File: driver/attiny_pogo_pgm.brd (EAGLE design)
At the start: 26.9 x 17.3 mm, 9 parts, among them IC1 ATTiny85, J1 AVR_SPI_PRG_6NS, P5V TPTP10R

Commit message: prepare for routing
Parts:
- removed IC1: ATTiny85, atmel:8S2
- moved JP1 9.60 mm to (11.3, 2.41), turned to 90 degrees
- moved J1 3.79 mm to (5.21, 3.68)
- moved PMOSI 3.69 mm to (2.29, 12.4)
- moved PSCK 3.69 mm to (2.29, 9.91)
- moved P5V 3.69 mm to (1.65, 8.64)
- moved PGND 3.69 mm to (9.02, 12.4)
- moved PMISO 3.69 mm to (1.65, 11.2)
- moved PRESET 3.69 mm to (9.02, 8.64)
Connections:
- net +5V: no longer IC1.8
- net GND: no longer IC1.4
- net IN1/MISO: no longer IC1.6
- net RESET-: no longer IC1.1
- net SCL/SCK: no longer IC1.7
- net SDA/MOSI: no longer IC1.5
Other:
- board size 26.9 x 17.3 mm -> 14.3 x 14.8 mm
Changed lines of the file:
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@@
 <board>
 <plain>
-<wire x1="0" y1="0" x2="26.904" y2="0" width="0" layer="20"/>
-<wire x1="26.904" y1="0" x2="26.904" y2="17.323" width="0" layer="20"/>
-<wire x1="26.904" y1="17.323" x2="0" y2="17.323" width="0" layer="20"/>
-<wire x1="0" y1="17.323" x2="0" y2="0" width="0" layer="20"/>
+<wire x1="0" y1="0" x2="14.331" y2="0" width="0" layer="20"/>
+<wire x1="14.331" y1="0" x2="14.331" y2="14.783" width="0" layer="20"/>
+<wire x1="14.331" y1="14.783" x2="0" y2="14.783" width="0" layer="20"/>
+<wire x1="0" y1="14.783" x2="0" y2="0" width="0" layer="20"/>
 </plain>
 <attributes>
@@
 </autorouter>
 <elements>
-<element name="IC1" library="atmel" package="8S2" value="ATTiny85" x="9.144" y="10.668" rot="R90">
-<attribute name="OC_NEWARK" value="96K6522" x="14.224" y="37.338" size="1.778" layer="27" rot="R90" display="off"/>
-<attribute name="MPN" value="ATTINY13-20SU" x="14.224" y="37.338" size="1.778" layer="27" rot="R90" display="off"/>
-<attribute name="MF" value="" x="14.224" y="37.338" size="1.778" layer="27" rot="R90" display="off"/>
-<attribute name="OC_FARNELL" value="9171568" x="14.224" y="37.338" size="1.778" layer="27" rot="R90" display="off"/>
-</element>
-<element name="J1" library="SparkFun-Connectors" package="2X3-NS" value="AVR_SPI_PRG_6NS" x="8.89" y="4.572"/>
-<element name="JP1" library="SparkFun-Connectors" package="1X02" value="" x="2.286" y="5.715" rot="R270"/>
-<element name="PMOSI" library="testpad" package="TP10R" value="TPTP10R" x="5.969" y="12.573">
-<attribute name="TP_SIGNAL_NAME" value="" x="5.969" y="12.573" size="1.778" layer="27" display="off"/>
-</element>
-<element name="PRESET" library="testpad" package="TP10R" value="TPTP10R" x="12.7" y="8.763">
-<attribute name="TP_SIGNAL_NAME" value="" x="12.7" y="8.763" size="1.778" layer="27" display="off"/>
-</element>
-<element name="PSCK" library="testpad" package="TP10R" value="TPTP10R" x="5.969" y="10.033">
-<attribute name="TP_SIGNAL_NAME" value="" x="5.969" y="10.033" size="1.778" layer="27" display="off"/>
-</element>
-<element name="PMISO" library="testpad" package="TP10R" value="TPTP10R" x="5.334" y="11.303">
-<attribute name="TP_SIGNAL_NAME" value="" x="5.334" y="11.303" size="1.778" layer="27" display="off"/>
-</element>
-<element name="PGND" library="testpad" package="TP10R" value="TPTP10R" x="12.7" y="12.573">
-<attribute name="TP_SIGNAL_NAME" value="" x="12.7" y="12.573" size="1.778" layer="27" display="off"/>
-</element>
-<element name="P5V" library="testpad" package="TP10R" value="TPTP10R" x="5.334" y="8.763">
-<attribute name="TP_SIGNAL_NAME" value="" x="5.334" y="8.763" size="1.778" layer="27" display="off"/>
+<element name="J1" library="SparkFun-Connectors" package="2X3-NS" value="AVR_SPI_PRG_6NS" x="5.207" y="3.683"/>
+<element name="JP1" library="SparkFun-Connectors" package="1X02" value="" x="11.303" y="2.413" rot="R90"/>
+<element name="PMOSI" library="testpad" package="TP10R" value="TPTP10R" x="2.286" y="12.446">
+<attribute name="TP_SIGNAL_NAME" value="" x="2.286" y="12.446" size="1.778" layer="27" display="off"/>
+</element>
+<element name="PRESET" library="testpad" package="TP10R" value="TPTP10R" x="9.017" y="8.636">
+<attribute name="TP_SIGNAL_NAME" value="" x="9.017" y="8.636" size="1.778" layer="27" display="off"/>
+</element>
+<element name="PSCK" library="testpad" package="TP10R" value="TPTP10R" x="2.286" y="9.906">
+<attribute name="TP_SIGNAL_NAME" value="" x="2.286" y="9.906" size="1.778" layer="27" display="off"/>
+</element>
+<element name="PMISO" library="testpad" package="TP10R" value="TPTP10R" x="1.651" y="11.176">
+<attribute name="TP_SIGNAL_NAME" value="" x="1.651" y="11.176" size="1.778" layer="27" display="off"/>
+</element>
+<element name="PGND" library="testpad" package="TP10R" value="TPTP10R" x="9.017" y="12.446">
+<attribute name="TP_SIGNAL_NAME" value="" x="9.017" y="12.446" size="1.778" layer="27" display="off"/>
+</element>
+<element name="P5V" library="testpad" package="TP10R" value="TPTP10R" x="1.651" y="8.636">
+<attribute name="TP_SIGNAL_NAME" value="" x="1.651" y="8.636" size="1.778" layer="27" display="off"/>
 </element>
 </elements>
 <signals>
 <signal name="IN1/MISO">
-<contactref element="IC1" pad="6"/>
 <contactref element="J1" pad="1"/>
 <contactref element="PMISO" pad="TP"/>
-<wire x1="5.334" y1="11.303" x2="5.74" y2="11.303" width="0" layer="19" extent="1-1"/>
-<wire x1="6.35" y1="3.302" x2="5.74" y2="11.303" width="0" layer="19" extent="1-1"/>
+<wire x1="2.667" y1="2.413" x2="1.651" y2="11.176" width="0" layer="19" extent="1-1"/>
 </signal>
 <signal name="GND">
-<contactref element="IC1" pad="4"/>
 <contactref element="J1" pad="6"/>
 <polygon width="0.2032" layer="1" isolate="0.4064">
@@
 </signal>
 <signal name="+5V">
-<contactref element="IC1" pad="8"/>
 <contactref element="J1" pad="2"/>
 <contactref element="JP1" pad="1"/>
 <contactref element="P5V" pad="TP"/>
-<wire x1="5.334" y1="8.763" x2="5.74" y2="8.763" width="0" layer="19" extent="1-1"/>
-<wire x1="6.35" y1="5.842" x2="5.74" y2="8.763" width="0" layer="19" extent="1-1"/>
-<wire x1="2.286" y1="5.715" x2="6.35" y2="5.842" width="0" layer="19" extent="1-1"/>
+<wire x1="2.667" y1="4.953" x2="11.303" y2="2.413" width="0" layer="19" extent="1-1"/>
+<wire x1="1.651" y1="8.636" x2="2.667" y2="4.953" width="0" layer="19" extent="1-1"/>
 </signal>
 <signal name="SDA/MOSI">
-<contactref element="IC1" pad="5"/>
 <contactref element="J1" pad="4"/>
 <contactref element="PMOSI" pad="TP"/>
-<wire x1="5.969" y1="12.573" x2="5.74" y2="12.573" width="0" layer="19" extent="1-1"/>
-<wire x1="8.89" y1="5.842" x2="5.969" y2="12.573" width="0" layer="19" extent="1-1"/>
+<wire x1="5.207" y1="4.953" x2="2.286" y2="12.446" width="0" layer="19" extent="1-1"/>
 </signal>
 <signal name="RESET-">
-<contactref element="IC1" pad="1"/>
 <contactref element="J1" pad="5"/>
 <contactref element="PRESET" pad="TP"/>
-<wire x1="12.548" y1="8.763" x2="12.7" y2="8.763" width="0" layer="19" extent="1-1"/>
-<wire x1="11.43" y1="3.302" x2="12.548" y2="8.763" width="0" layer="19" extent="1-1"/>
+<wire x1="7.747" y1="2.413" x2="9.017" y2="8.636" width="0" layer="19" extent="1-1"/>
 </signal>
 <signal name="SCL/SCK">
-<contactref element="IC1" pad="7"/>
 <contactref element="J1" pad="3"/>
 <contactref element="PSCK" pad="TP"/>
-<wire x1="5.969" y1="10.033" x2="5.74" y2="10.033" width="0" layer="19" extent="1-1"/>
-<wire x1="8.89" y1="3.302" x2="5.969" y2="10.033" width="0" layer="19" extent="1-1"/>
+<wire x1="5.207" y1="2.413" x2="2.286" y2="9.906" width="0" layer="19" extent="1-1"/>
 </signal>
 </signals>

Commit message: routed
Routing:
- net IN1/MISO: track 0.00 -> 25.4 mm
- net +5V: track 0.00 -> 20.6 mm
- net GND: track 0.00 -> 15.9 mm
- net SCL/SCK: track 0.00 -> 8.70 mm
- net SDA/MOSI: track 0.00 -> 8.70 mm
- net RESET-: track 0.00 -> 6.75 mm
- removed copper zone on layer 1, net GND
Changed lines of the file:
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@@
 <param name="RoutingGrid" value="2.5mil"/>
 <param name="tpViaShape" value="round"/>
-<param name="PrefDir.1" value="-"/>
+<param name="PrefDir.1" value="|"/>
 <param name="PrefDir.2" value="0"/>
 <param name="PrefDir.3" value="0"/>
@@
 <contactref element="J1" pad="1"/>
 <contactref element="PMISO" pad="TP"/>
-<wire x1="2.667" y1="2.413" x2="1.651" y2="11.176" width="0" layer="19" extent="1-1"/>
+<wire x1="1.4605" y1="11.3665" x2="1.651" y2="11.176" width="0.2032" layer="1"/>
+<wire x1="0.8255" y1="12.2555" x2="1.4605" y2="11.3665" width="0.2032" layer="1"/>
+<wire x1="1.3335" y1="13.6525" x2="0.8255" y2="12.2555" width="0.2032" layer="1"/>
+<wire x1="6.477" y1="13.6525" x2="1.3335" y2="13.6525" width="0.2032" layer="1"/>
+<wire x1="6.477" y1="1.905" x2="6.477" y2="13.6525" width="0.2032" layer="1"/>
+<wire x1="5.715" y1="1.016" x2="6.477" y2="1.905" width="0.2032" layer="1"/>
+<wire x1="2.667" y1="1.016" x2="5.715" y2="1.016" width="0.2032" layer="1"/>
+<wire x1="2.667" y1="2.413" x2="2.667" y2="1.016" width="0.2032" layer="1"/>
 </signal>
 <signal name="GND">
 <contactref element="J1" pad="6"/>
-<polygon width="0.2032" layer="1" isolate="0.4064">
-<vertex x="0" y="16.256"/>
-<vertex x="0" y="0"/>
-<vertex x="26.924" y="0"/>
-<vertex x="26.924" y="16.256"/>
-</polygon>
 <contactref element="JP1" pad="2"/>
 <contactref element="PGND" pad="TP"/>
+<wire x1="7.747" y1="11.176" x2="9.017" y2="12.446" width="0.2032" layer="1"/>
+<wire x1="7.747" y1="4.953" x2="7.747" y2="10.9855" width="0.2032" layer="1"/>
+<wire x1="7.747" y1="10.9855" x2="7.747" y2="11.176" width="0.2032" layer="1"/>
+<wire x1="10.4775" y1="6.5405" x2="11.303" y2="4.953" width="0.2032" layer="1"/>
+<wire x1="10.4775" y1="9.5885" x2="10.4775" y2="6.5405" width="0.2032" layer="1"/>
+<wire x1="7.8105" y1="10.9855" x2="10.4775" y2="9.5885" width="0.2032" layer="1"/>
+<wire x1="7.8105" y1="10.9855" x2="7.747" y2="10.9855" width="0.2032" layer="1"/>
 </signal>
 <signal name="+5V">
@@
 <contactref element="JP1" pad="1"/>
 <contactref element="P5V" pad="TP"/>
-<wire x1="2.667" y1="4.953" x2="11.303" y2="2.413" width="0" layer="19" extent="1-1"/>
-<wire x1="1.651" y1="8.636" x2="2.667" y2="4.953" width="0" layer="19" extent="1-1"/>
+<wire x1="2.667" y1="7.62" x2="1.651" y2="8.636" width="0.2032" layer="1"/>
+<wire x1="2.667" y1="4.953" x2="2.667" y2="7.62" width="0.2032" layer="1"/>
+<wire x1="11.303" y1="2.413" x2="11.303" y2="1.651" width="0.2032" layer="1"/>
+<wire x1="11.303" y1="1.651" x2="10.16" y2="0.508" width="0.2032" layer="1"/>
+<wire x1="10.16" y1="0.508" x2="1.651" y2="0.508" width="0.2032" layer="1"/>
+<wire x1="1.651" y1="0.508" x2="0.762" y2="1.397" width="0.2032" layer="1"/>
+<wire x1="0.762" y1="1.397" x2="0.762" y2="3.048" width="0.2032" layer="1"/>
+<wire x1="0.762" y1="3.048" x2="2.667" y2="4.953" width="0.2032" layer="1"/>
 </signal>
 <signal name="SDA/MOSI">
 <contactref element="J1" pad="4"/>
 <contactref element="PMOSI" pad="TP"/>
-<wire x1="5.207" y1="4.953" x2="2.286" y2="12.446" width="0" layer="19" extent="1-1"/>
+<wire x1="5.207" y1="9.525" x2="2.286" y2="12.446" width="0.2032" layer="1"/>
+<wire x1="5.207" y1="4.953" x2="5.207" y2="9.525" width="0.2032" layer="1"/>
 </signal>
 <signal name="RESET-">
 <contactref element="J1" pad="5"/>
 <contactref element="PRESET" pad="TP"/>
-<wire x1="7.747" y1="2.413" x2="9.017" y2="8.636" width="0" layer="19" extent="1-1"/>
+<wire x1="9.017" y1="3.683" x2="9.017" y2="8.636" width="0.2032" layer="1"/>
+<wire x1="7.747" y1="2.413" x2="9.017" y2="3.683" width="0.2032" layer="1"/>
 </signal>
 <signal name="SCL/SCK">
 <contactref element="J1" pad="3"/>
 <contactref element="PSCK" pad="TP"/>
-<wire x1="5.207" y1="2.413" x2="2.286" y2="9.906" width="0" layer="19" extent="1-1"/>
+<wire x1="3.937" y1="8.255" x2="2.286" y2="9.906" width="0.2032" layer="1"/>
+<wire x1="3.937" y1="3.683" x2="3.937" y2="8.255" width="0.2032" layer="1"/>
+<wire x1="5.207" y1="2.413" x2="3.937" y2="3.683" width="0.2032" layer="1"/>
 </signal>
 </signals>

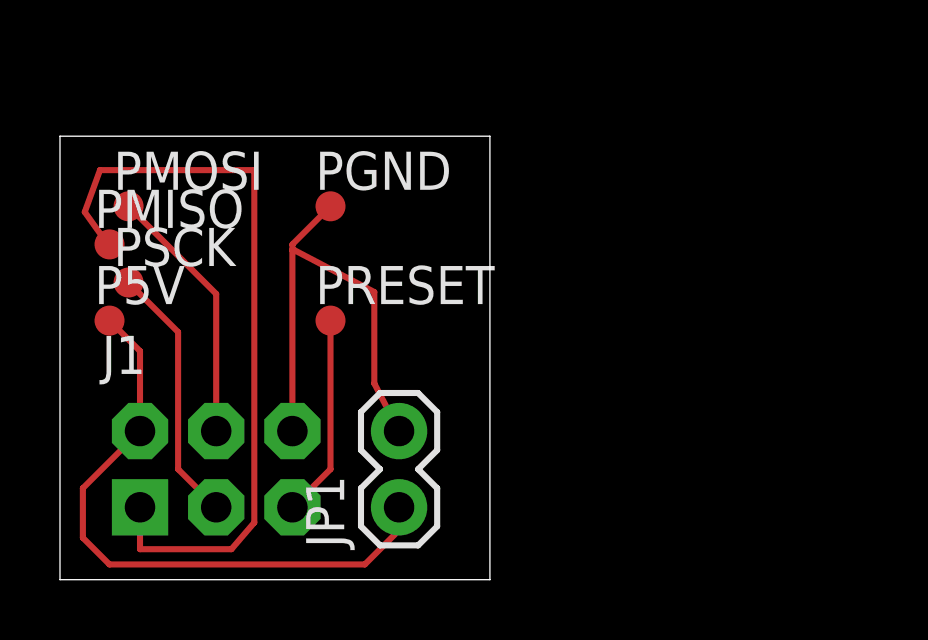
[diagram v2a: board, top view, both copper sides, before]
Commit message: use slightly bigger pads for the pogo pins
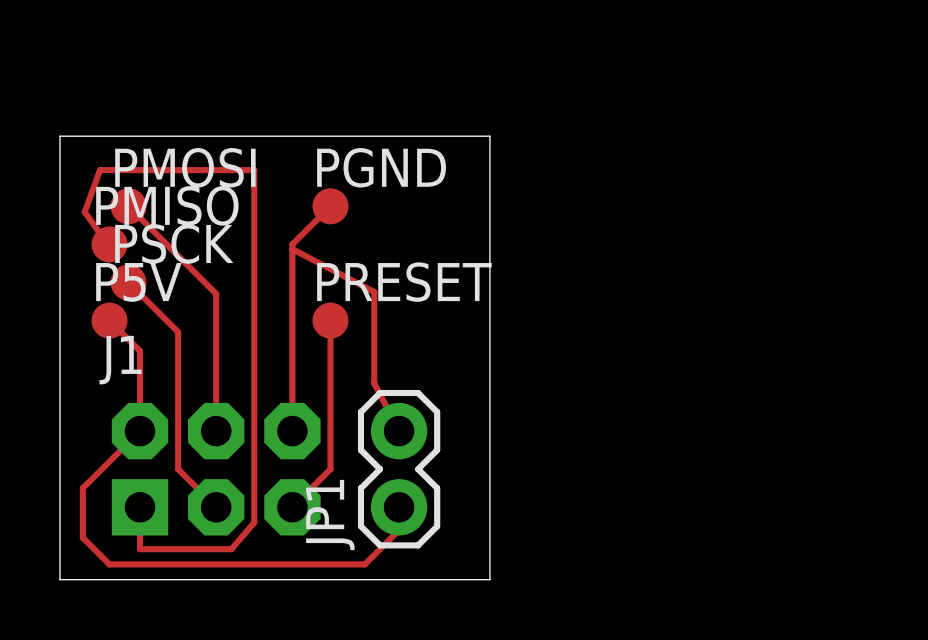
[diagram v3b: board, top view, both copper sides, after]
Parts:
- P5V, PGND, PMISO, PMOSI, PRESET, PSCK: value TPTP10R -> TPTP12R; device testpad:TP10R -> testpad:TP12R
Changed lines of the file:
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@@
 <element name="J1" library="SparkFun-Connectors" package="2X3-NS" value="AVR_SPI_PRG_6NS" x="5.207" y="3.683"/>
 <element name="JP1" library="SparkFun-Connectors" package="1X02" value="" x="11.303" y="2.413" rot="R90"/>
-<element name="PMOSI" library="testpad" package="TP10R" value="TPTP10R" x="2.286" y="12.446">
+<element name="PMOSI" library="testpad" package="TP12R" value="TPTP12R" x="2.286" y="12.446">
 <attribute name="TP_SIGNAL_NAME" value="" x="2.286" y="12.446" size="1.778" layer="27" display="off"/>
 </element>
-<element name="PRESET" library="testpad" package="TP10R" value="TPTP10R" x="9.017" y="8.636">
+<element name="PMISO" library="testpad" package="TP12R" value="TPTP12R" x="1.651" y="11.176">
+<attribute name="TP_SIGNAL_NAME" value="" x="1.651" y="11.176" size="1.778" layer="27" display="off"/>
+</element>
+<element name="PSCK" library="testpad" package="TP12R" value="TPTP12R" x="2.286" y="9.906">
+<attribute name="TP_SIGNAL_NAME" value="" x="2.286" y="9.906" size="1.778" layer="27" display="off"/>
+</element>
+<element name="PRESET" library="testpad" package="TP12R" value="TPTP12R" x="9.017" y="8.636">
 <attribute name="TP_SIGNAL_NAME" value="" x="9.017" y="8.636" size="1.778" layer="27" display="off"/>
 </element>
-<element name="PSCK" library="testpad" package="TP10R" value="TPTP10R" x="2.286" y="9.906">
-<attribute name="TP_SIGNAL_NAME" value="" x="2.286" y="9.906" size="1.778" layer="27" display="off"/>
-</element>
-<element name="PMISO" library="testpad" package="TP10R" value="TPTP10R" x="1.651" y="11.176">
-<attribute name="TP_SIGNAL_NAME" value="" x="1.651" y="11.176" size="1.778" layer="27" display="off"/>
-</element>
-<element name="PGND" library="testpad" package="TP10R" value="TPTP10R" x="9.017" y="12.446">
+<element name="PGND" library="testpad" package="TP12R" value="TPTP12R" x="9.017" y="12.446">
 <attribute name="TP_SIGNAL_NAME" value="" x="9.017" y="12.446" size="1.778" layer="27" display="off"/>
 </element>
-<element name="P5V" library="testpad" package="TP10R" value="TPTP10R" x="1.651" y="8.636">
+<element name="P5V" library="testpad" package="TP12R" value="TPTP12R" x="1.651" y="8.636">
 <attribute name="TP_SIGNAL_NAME" value="" x="1.651" y="8.636" size="1.778" layer="27" display="off"/>
 </element>
@@
 <signal name="IN1/MISO">
 <contactref element="J1" pad="1"/>
-<contactref element="PMISO" pad="TP"/>
 <wire x1="1.4605" y1="11.3665" x2="1.651" y2="11.176" width="0.2032" layer="1"/>
 <wire x1="0.8255" y1="12.2555" x2="1.4605" y2="11.3665" width="0.2032" layer="1"/>
@@
 <wire x1="2.667" y1="1.016" x2="5.715" y2="1.016" width="0.2032" layer="1"/>
 <wire x1="2.667" y1="2.413" x2="2.667" y2="1.016" width="0.2032" layer="1"/>
+<contactref element="PMISO" pad="TP"/>
 </signal>
 <signal name="GND">
 <contactref element="J1" pad="6"/>
 <contactref element="JP1" pad="2"/>
-<contactref element="PGND" pad="TP"/>
 <wire x1="7.747" y1="11.176" x2="9.017" y2="12.446" width="0.2032" layer="1"/>
 <wire x1="7.747" y1="4.953" x2="7.747" y2="10.9855" width="0.2032" layer="1"/>
@@
 <wire x1="7.8105" y1="10.9855" x2="10.4775" y2="9.5885" width="0.2032" layer="1"/>
 <wire x1="7.8105" y1="10.9855" x2="7.747" y2="10.9855" width="0.2032" layer="1"/>
+<contactref element="PGND" pad="TP"/>
 </signal>
 <signal name="+5V">
 <contactref element="J1" pad="2"/>
 <contactref element="JP1" pad="1"/>
-<contactref element="P5V" pad="TP"/>
 <wire x1="2.667" y1="7.62" x2="1.651" y2="8.636" width="0.2032" layer="1"/>
 <wire x1="2.667" y1="4.953" x2="2.667" y2="7.62" width="0.2032" layer="1"/>
@@
 <wire x1="0.762" y1="1.397" x2="0.762" y2="3.048" width="0.2032" layer="1"/>
 <wire x1="0.762" y1="3.048" x2="2.667" y2="4.953" width="0.2032" layer="1"/>
+<contactref element="P5V" pad="TP"/>
 </signal>
 <signal name="SDA/MOSI">
 <contactref element="J1" pad="4"/>
-<contactref element="PMOSI" pad="TP"/>
 <wire x1="5.207" y1="9.525" x2="2.286" y2="12.446" width="0.2032" layer="1"/>
 <wire x1="5.207" y1="4.953" x2="5.207" y2="9.525" width="0.2032" layer="1"/>
+<contactref element="PMOSI" pad="TP"/>
 </signal>
 <signal name="RESET-">
 <contactref element="J1" pad="5"/>
-<contactref element="PRESET" pad="TP"/>
 <wire x1="9.017" y1="3.683" x2="9.017" y2="8.636" width="0.2032" layer="1"/>
 <wire x1="7.747" y1="2.413" x2="9.017" y2="3.683" width="0.2032" layer="1"/>
+<contactref element="PRESET" pad="TP"/>
 </signal>
 <signal name="SCL/SCK">
 <contactref element="J1" pad="3"/>
-<contactref element="PSCK" pad="TP"/>
 <wire x1="3.937" y1="8.255" x2="2.286" y2="9.906" width="0.2032" layer="1"/>
 <wire x1="3.937" y1="3.683" x2="3.937" y2="8.255" width="0.2032" layer="1"/>
 <wire x1="5.207" y1="2.413" x2="3.937" y2="3.683" width="0.2032" layer="1"/>
+<contactref element="PSCK" pad="TP"/>
 </signal>
 </signals>
